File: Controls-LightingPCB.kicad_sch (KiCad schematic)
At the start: 30 parts, among them J1 PeripheralCANConnector, J2 PeripheralCANConnector, U1 PeripheralSOM

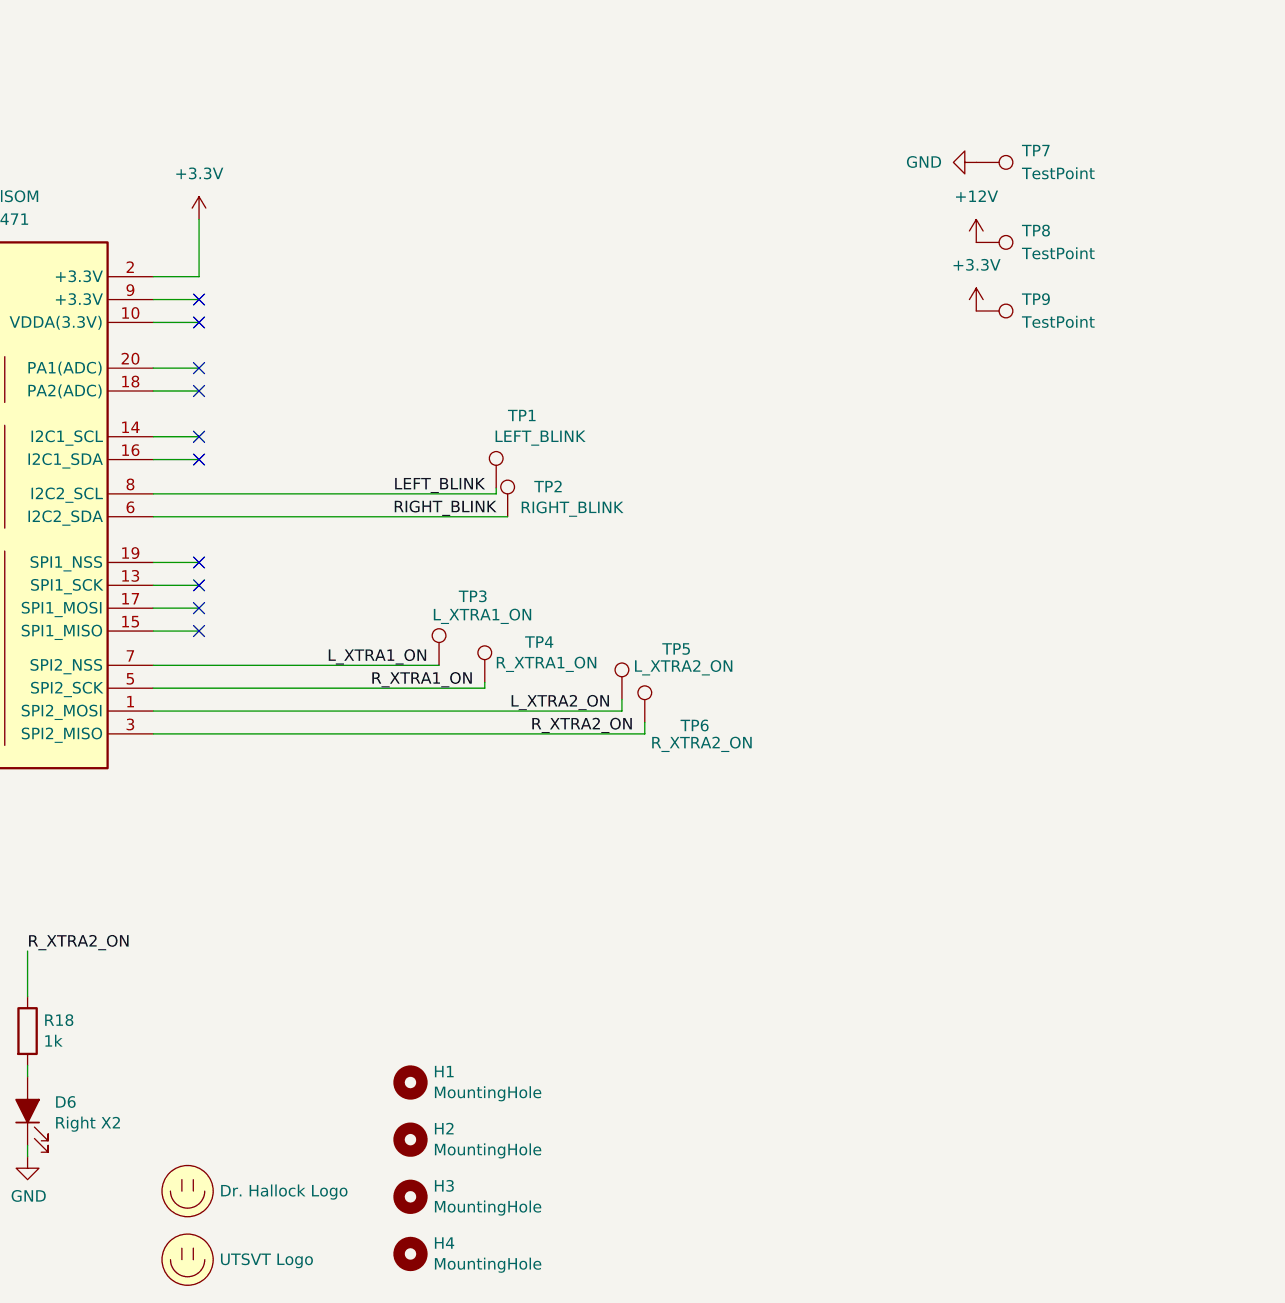
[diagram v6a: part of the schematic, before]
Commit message: layout before connecting traces
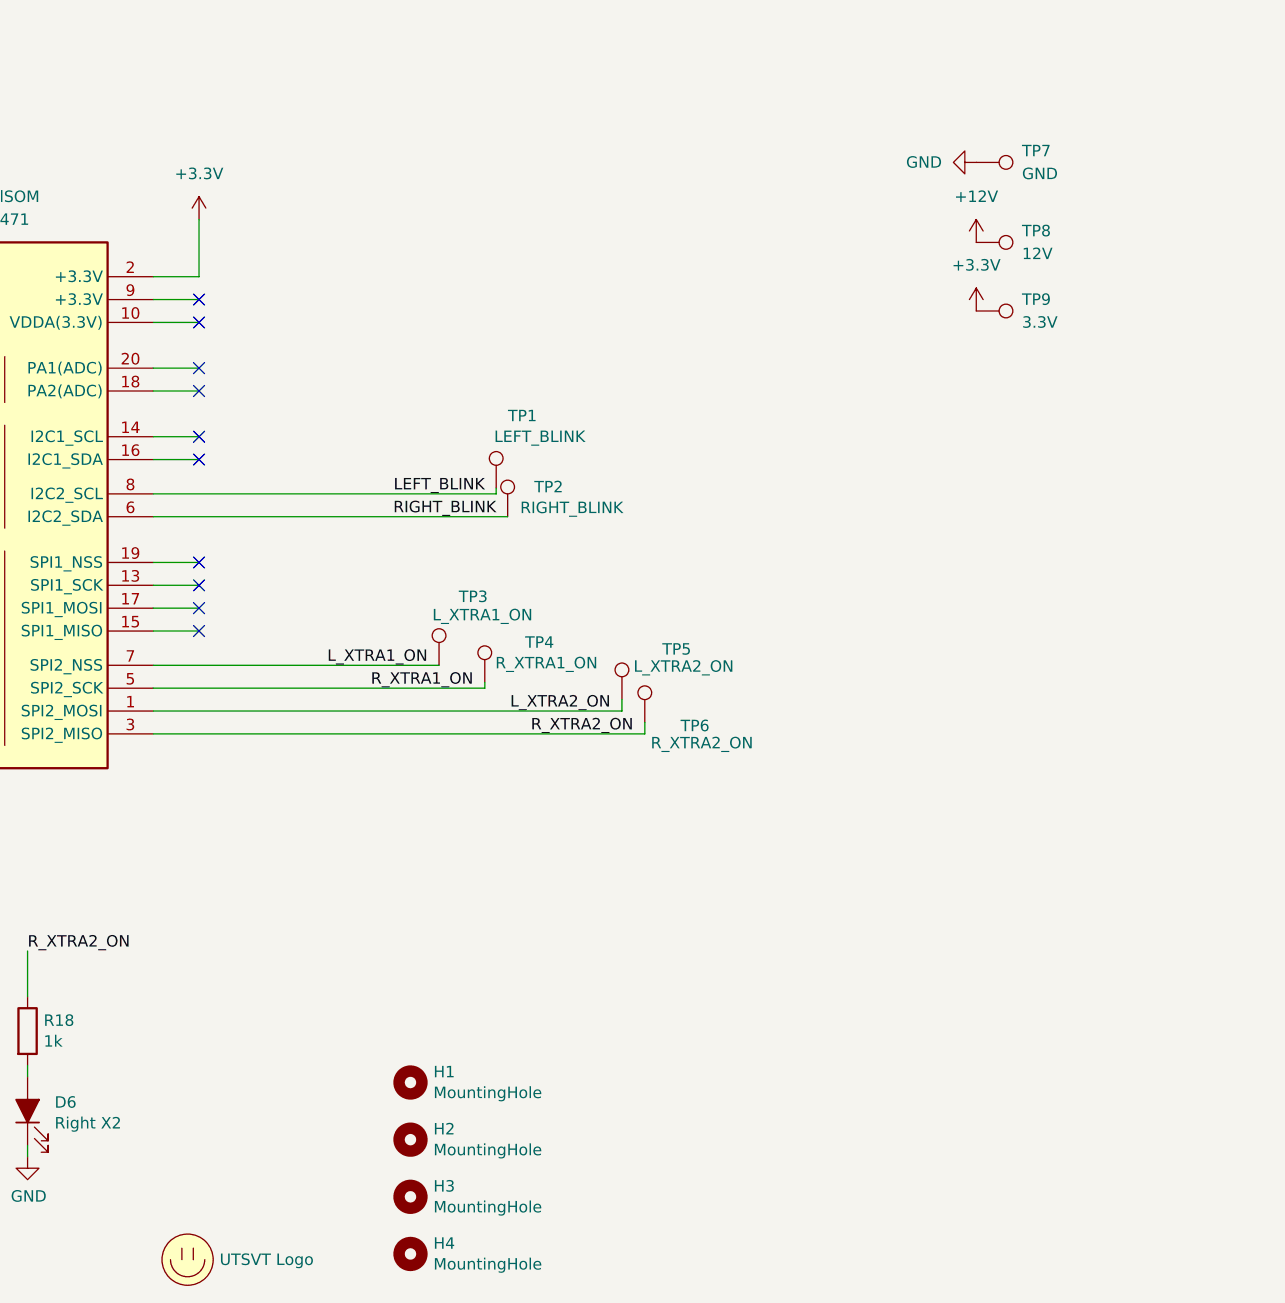
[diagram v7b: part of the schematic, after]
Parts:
- removed LOGO1: Dr. Hallock Logo, UTSVT_Special:Hallock_Image_Small, symbol Controls-LightingPCB-rescue:Logo_Placeholder-utsvt-misc
- TP7: value TestPoint -> GND
- TP8: value TestPoint -> 12V
- TP9: value TestPoint -> 3.3V
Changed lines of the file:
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@@
-	)
-	(symbol
-		(lib_id "Controls-LightingPCB-rescue:Logo_Placeholder-utsvt-misc")
-		(at 129.54 184.15 0)
-		(unit 1)
-		(exclude_from_sim no)
-		(in_bom yes)
-		(on_board yes)
-		(dnp no)
-		(property "Reference" "LOGO1"
-			(at 129.54 180.34 0)
-			(effects
-				(font
-					(size 1.27 1.27)
-				)
-				(hide yes)
-			)
-		)
-		(property "Value" "Dr. Hallock Logo"
-			(at 133.096 184.15 0)
-			(effects
-				(font
-					(size 1.27 1.27)
-				)
-				(justify left)
-			)
-		)
-		(property "Footprint" "UTSVT_Special:Hallock_Image_Small"
-			(at 129.54 182.245 0)
-			(effects
-				(font
-					(size 1.27 1.27)
-				)
-				(hide yes)
-			)
-		)
-		(property "Datasheet" ""
-			(at 129.54 182.245 0)
-			(effects
-				(font
-					(size 1.27 1.27)
-				)
-				(hide yes)
-			)
-		)
-		(property "Description" ""
-			(at 129.54 184.15 0)
-			(effects
-				(font
-					(size 1.27 1.27)
-				)
-				(hide yes)
-			)
-		)
-		(instances
-			(project "Controls-LightingPCB"
-				(path "/229b82f0-5048-47d6-8bc8-0bcee42eb4bc"
-					(reference "LOGO1")
-					(unit 1)
-				)
-			)
-		)
 	)
 	(symbol
@@
 			)
 		)
-		(property "Value" "TestPoint"
+		(property "Value" "12V"
 			(at 222.25 80.0099 90)
 			(effects
@@
 			)
 		)
-		(property "Value" "TestPoint"
+		(property "Value" "GND"
 			(at 222.25 71.1199 90)
 			(effects
@@
 			)
 		)
-		(property "Value" "TestPoint"
+		(property "Value" "3.3V"
 			(at 222.25 87.6299 90)
 			(effects

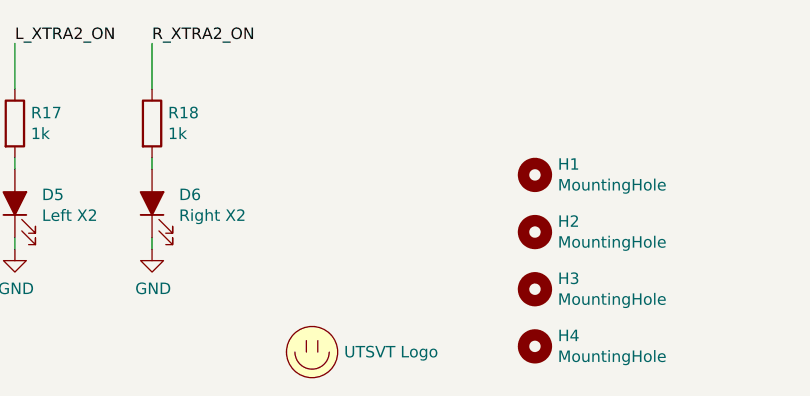
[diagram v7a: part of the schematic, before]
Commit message: moved mounting holes inward
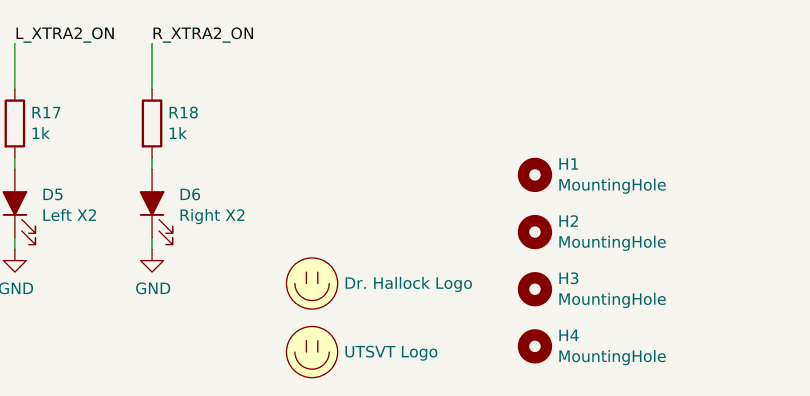
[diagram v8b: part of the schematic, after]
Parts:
- added LOGO1: Dr. Hallock Logo, UTSVT_Special:Hallock_Image_Small, symbol Controls-LightingPCB-rescue:Logo_Placeholder-utsvt-misc
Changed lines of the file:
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@@
+	)
+	(symbol
+		(lib_id "Controls-LightingPCB-rescue:Logo_Placeholder-utsvt-misc")
+		(at 129.54 184.15 0)
+		(unit 1)
+		(exclude_from_sim no)
+		(in_bom yes)
+		(on_board yes)
+		(dnp no)
+		(property "Reference" "LOGO1"
+			(at 129.54 180.34 0)
+			(effects
+				(font
+					(size 1.27 1.27)
+				)
+				(hide yes)
+			)
+		)
+		(property "Value" "Dr. Hallock Logo"
+			(at 133.096 184.15 0)
+			(effects
+				(font
+					(size 1.27 1.27)
+				)
+				(justify left)
+			)
+		)
+		(property "Footprint" "UTSVT_Special:Hallock_Image_Small"
+			(at 129.54 182.245 0)
+			(effects
+				(font
+					(size 1.27 1.27)
+				)
+				(hide yes)
+			)
+		)
+		(property "Datasheet" ""
+			(at 129.54 182.245 0)
+			(effects
+				(font
+					(size 1.27 1.27)
+				)
+				(hide yes)
+			)
+		)
+		(property "Description" ""
+			(at 129.54 184.15 0)
+			(effects
+				(font
+					(size 1.27 1.27)
+				)
+				(hide yes)
+			)
+		)
+		(instances
+			(project "Controls-LightingPCB"
+				(path "/229b82f0-5048-47d6-8bc8-0bcee42eb4bc"
+					(reference "LOGO1")
+					(unit 1)
+				)
+			)
+		)
 	)
 	(symbol
